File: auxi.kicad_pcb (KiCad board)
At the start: 2 copper layers, 90 x 100 mm, 49 parts

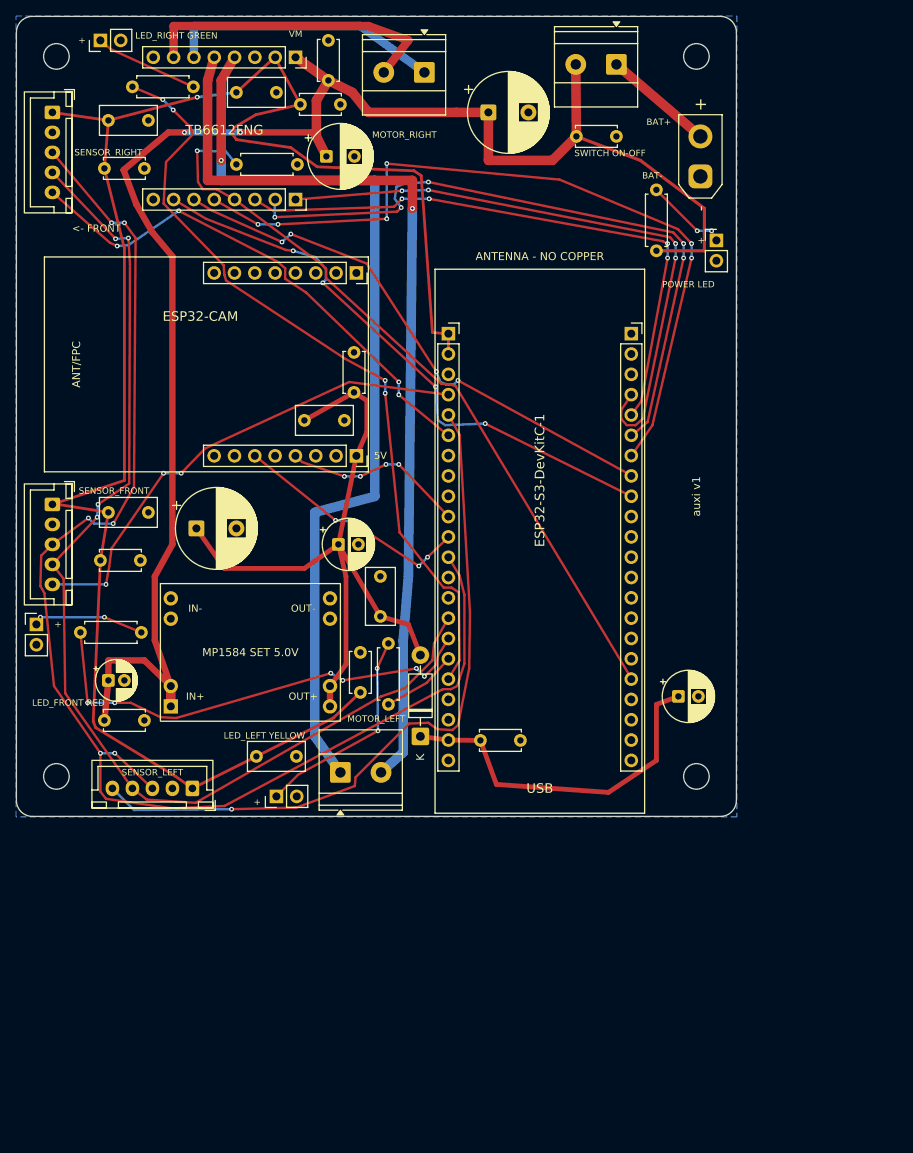
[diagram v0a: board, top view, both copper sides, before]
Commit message: feat(pcb): single-layer 110 x 140 mm board with GND pour, soldered from below
Re-do the PCB as a one-copper-layer board for home etching and hand drilling:

- Copper only on B.Cu with a GND pour; F.Cu has no copper (keepout over the
  whole top face). All parts are THT, mounted on top and soldered from below.
  No vias and no jumper wires: no two tracks cross.
- Board outline 110 x 140 mm (was 90 x 100 mm), M3 holes 5 mm from the corners,
  antenna keepouts for the ESP32-S3 and the ESP32-CAM.
- Track width >= 0.4 mm (0.3 mm only between pads / tight bundles), clearance
  0.2 mm, smallest hole 0.3 mm, default via 1.1 / 0.3 mm. Pad diameter = drill
  + 0.8 mm on every pad hole, enforced by auxi.kicad_dru. Four standard
  footprints copied into auxi.pretty with bigger pads.
- GPIOs reassigned so the signals leave the ESP32 headers in the order of their
  destinations (I2C on GPIO4/5, XSHUT 6/7/15, LEDs 8/9/10, motor signals
  reversed on J3). Schematic updated, ERC clean.
- DRC: 0 violations, 0 unconnected items.
- README.md and CLAUDE.md updated; regenerated schematic PDF, BOM, 1:1 print
  PDF (top, copper, mirrored copper) and renders.

Co-Authored-By: Claude Sonnet 5.5 <noreply@anthropic.com>
Claude-Session: https://claude.ai/code/session_01V1Casvb8MJmuQffuKiRczF
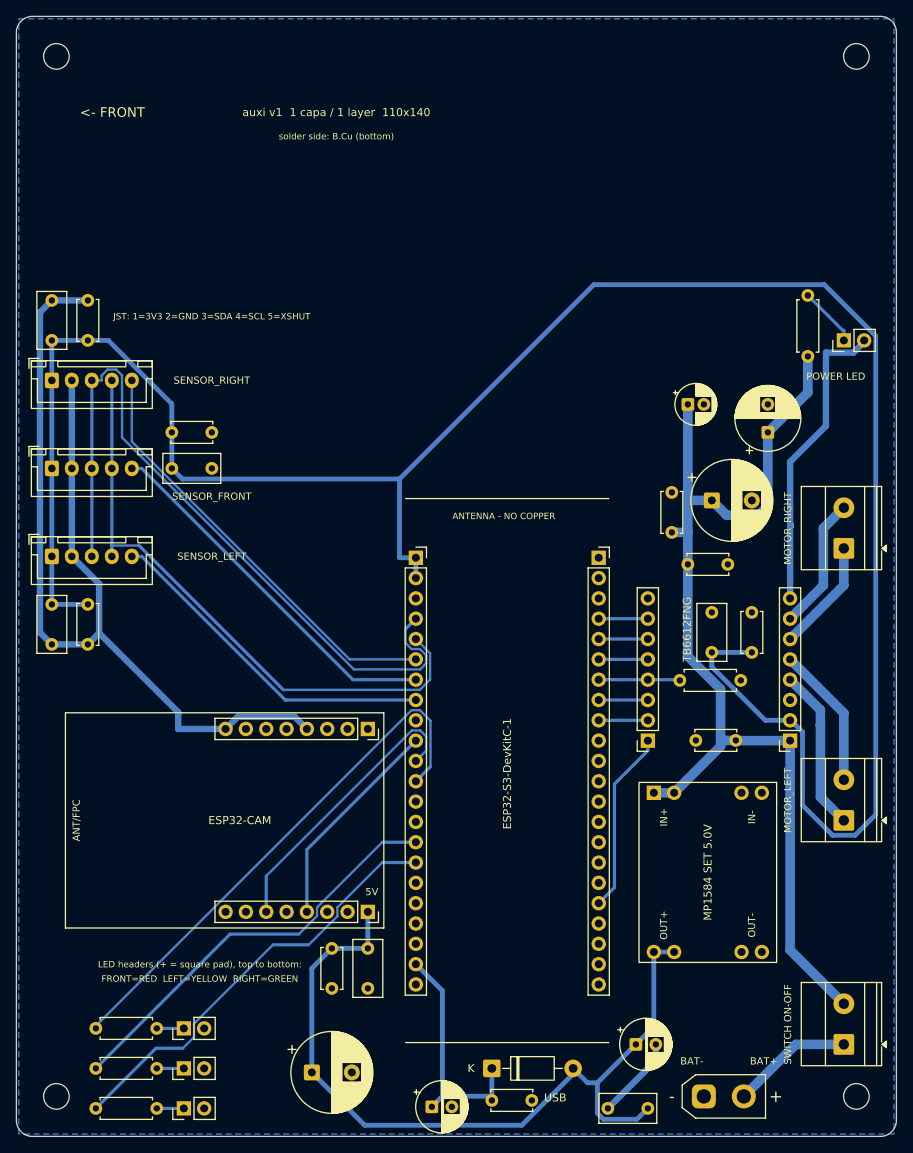
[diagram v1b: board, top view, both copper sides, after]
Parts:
- J_LED_FRONT1, J_LED_LEFT1, J_LED_POWER1, J_LED_RIGHT1: footprint Connector_PinHeader_2.54mm:PinHeader_1x02_P2.54mm_Vertical -> auxi:PinHeader_1x02_P2.54mm_Vertical
- J_SENSOR_FRONT1, J_SENSOR_LEFT1, J_SENSOR_RIGHT1: footprint Connector_JST:JST_XH_B5B-XH-A_1x05_P2.50mm_Vertical -> auxi:JST_XH_B5B-XH-A_1x05_P2.50mm_Vertical
- U_CAM1, U_CAM2, U_TB1, U_TB2: footprint Connector_PinSocket_2.54mm:PinSocket_1x08_P2.54mm_Vertical -> auxi:PinSocket_1x08_P2.54mm_Vertical
- U_ESP_J1, U_ESP_J3: footprint Connector_PinSocket_2.54mm:PinSocket_1x22_P2.54mm_Vertical -> auxi:PinSocket_1x22_P2.54mm_Vertical
- moved J_LED_RIGHT1 133.9 mm to (127.0, 184.0)
- moved R5 127.8 mm to (116.0, 184.0)
- moved J_SWITCH1 125.8 mm to (209.5, 176.0), turned to 90 degrees
- moved J_BAT1 115.0 mm to (192.0, 182.5), turned to 0 degrees
- moved U_TB2 105.4 mm to (202.8, 138.0), turned to 180 degrees
- moved C4 97.0 mm to (196.0, 138.0), turned to 180 degrees
- moved C14 91.8 mm to (193.0, 127.0), turned to 90 degrees
- moved C15 88.8 mm to (198.0, 127.0), turned to 90 degrees
- moved R2 85.0 mm to (189.0, 130.5)
- moved U_TB1 80.7 mm to (185.0, 138.0), turned to 180 degrees
- moved C5 80.2 mm to (190.0, 96.0)
- moved J_MOTOR_RIGHT1 79.3 mm to (209.5, 114.0), turned to 90 degrees
- moved C6 74.7 mm to (188.0, 112.0), turned to 90 degrees
- moved C7 72.7 mm to (183.5, 176.0)
- moved C8 70.0 mm to (185.0, 184.0), turned to 180 degrees
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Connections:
- U_ESP_J1 pad 12: SDA -> LED_FRONT
- U_ESP_J1 pad 15: SCL -> LED_LEFT
- U_ESP_J1 pad 16: LED_FRONT -> LED_RIGHT
- U_ESP_J1 pad 17: LED_LEFT -> (no net)
- U_ESP_J1 pad 18: LED_RIGHT -> (no net)
- U_ESP_J1 pad 4: XSHUT_FRONT -> SDA
- U_ESP_J1 pad 5: XSHUT_LEFT -> SCL
- U_ESP_J1 pad 7: (no net) -> XSHUT_FRONT
- U_ESP_J1 pad 8: (no net) -> XSHUT_LEFT
- U_ESP_J3 pad 18: STBY -> PWMA
- U_ESP_J3 pad 4: PWMA -> PWMB
- U_ESP_J3 pad 5: AIN1 -> BIN2
- U_ESP_J3 pad 6: AIN2 -> BIN1
- U_ESP_J3 pad 7: BIN1 -> STBY
- U_ESP_J3 pad 8: BIN2 -> AIN1
- U_ESP_J3 pad 9: PWMB -> AIN2
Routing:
- net GND: track 0.00 -> 170.2 mm
- net M_L2: track 116.4 -> 17.8 mm, vias 1 -> 0
- net M_L1: track 115.8 -> 20.4 mm, vias 1 -> 0
- net BIN1: track 97.4 -> 6.14 mm, vias 6 -> 0
- net STBY: track 94.5 -> 10.2 mm, vias 1 -> 0
- net AIN2: track 83.7 -> 6.14 mm, vias 5 -> 0
- net +VBAT_SW: track 209.0 -> 133.6 mm, vias 2 -> 0
- net SDA: track 168.1 -> 92.9 mm, vias 6 -> 0
- net AIN1: track 75.0 -> 6.14 mm, vias 4 -> 0
- net PWMB: track 73.0 -> 6.14 mm, vias 4 -> 0
- net SCL: track 138.3 -> 75.6 mm, vias 4 -> 0
- net BIN2: track 68.6 -> 6.14 mm, vias 4 -> 0
- net +3V3: track 222.5 -> 281.8 mm, vias 1 -> 0
- net PWMA: track 77.6 -> 22.9 mm, vias 4 -> 0
- net XSHUT_LEFT: track 88.4 -> 42.9 mm, vias 1 -> 0
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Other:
- board size 90 x 100 mm -> 110 x 140 mm
- board text added: "FRONT=RED LEFT=YELLOW RIGHT=GREEN"
- board text added: "JST: 1=3V3 2=GND 3=SDA 4=SCL 5=XSHUT"
- board text added: "LED headers (+ = square pad), top to bottom:"
- board text added: "auxi v1 1 capa / 1 layer 110x140"
- board text added: "solder side: B.Cu (bottom)"
- board text removed: "+"
- board text removed: "LED_FRONT RED"
- board text removed: "LED_LEFT YELLOW"
- board text removed: "LED_RIGHT GREEN"
- board text removed: "VM"
- board text removed: "auxi v1"

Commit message: feat(pcb): spread the components over the whole board
The first single-layer layout left the top third of the board empty and
crowded the parts toward the bottom edge. The logic block (ESP32-S3, ESP32-CAM,
TB6612FNG, MP1584) moves 26 mm north, the three sensor connectors get a 14 mm
pitch, the power capacitors and the motor/LED connectors use the upper right
corner, and the LED headers, big capacitors, diode, battery and switch are
spaced along the bottom.

- Re-routed on one layer: 224 tracks, 0 vias, no jumper wires.
- DRC: 0 violations, 0 unconnected items. ERC clean. PCB nets match the
  schematic pin by pin. Pin mapping unchanged from the previous commit.
- 55 tracks (377 mm) stay at 0.3 mm where they squeeze between pads.
- README.md, CLAUDE.md and the 1:1 PDF / renders regenerated.

Co-Authored-By: Claude Sonnet 5.5 <noreply@anthropic.com>
Claude-Session: https://claude.ai/code/session_01V1Casvb8MJmuQffuKiRczF
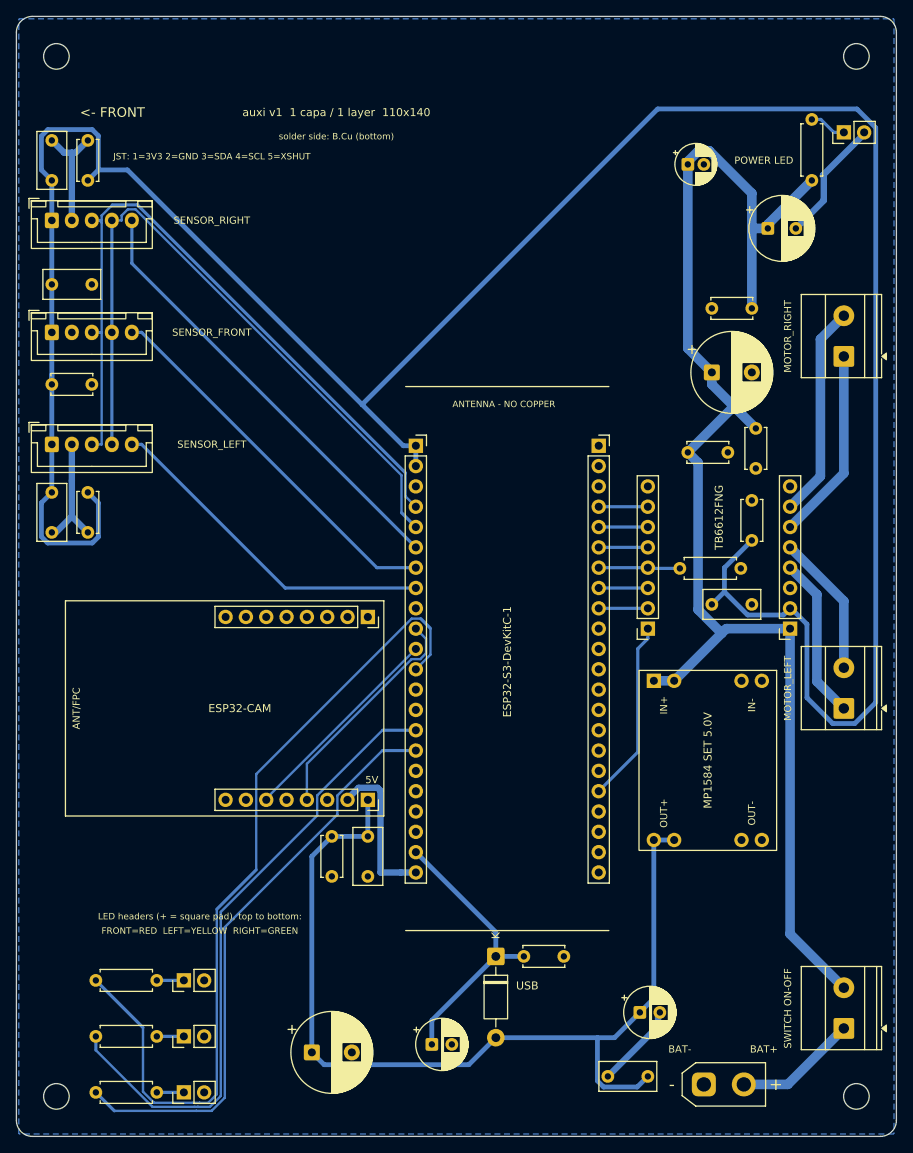
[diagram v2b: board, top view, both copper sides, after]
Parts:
- moved C4 39.1 mm to (198.5, 99.0), turned to -90 degrees
- moved C5 30.0 mm to (190.0, 66.0)
- moved C6 29.7 mm to (198.0, 84.0), turned to 180 degrees
- moved C16 27.5 mm to (110.5, 81.0)
- moved J_LED_POWER1 26.0 mm to (209.5, 62.0)
- moved C3 25.5 mm to (200.0, 74.0), turned to 0 degrees
- moved J_MOTOR_RIGHT1 24.0 mm to (209.5, 90.0)
- moved R1 22.0 mm to (205.5, 68.0)
- moved C20 20.0 mm to (110.5, 68.0)
- moved C21 20.0 mm to (115.0, 68.0)
- moved J_SENSOR_RIGHT1 20.0 mm to (110.5, 73.0)
- moved C10 18.4 mm to (169.5, 165.0)
- moved J_SENSOR_FRONT1 17.0 mm to (110.5, 87.0)
- moved C17 16.2 mm to (110.5, 93.5)
- moved C1 16.0 mm to (193.0, 92.0)
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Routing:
- net GND: track 170.2 -> 75.4 mm
- net +3V3: track 281.8 -> 331.9 mm
- net +VBAT_SW: track 133.6 -> 172.2 mm
- net LED_FRONT: track 67.4 -> 104.9 mm
- net LED_LEFT: track 52.3 -> 79.1 mm
- net LED_RIGHT: track 54.4 -> 73.5 mm
- net +5V: track 100.9 -> 118.8 mm
- net SCL: track 75.6 -> 86.1 mm
- net M_R1: track 16.7 -> 26.7 mm
- net M_R2: track 14.1 -> 24.1 mm
- net UART_CAM_TO_ESP: track 35.9 -> 26.6 mm
- net +5V_ESP: track 29.9 -> 35.0 mm
- net LED_POWER_A: track 7.56 -> 4.67 mm
- net SDA: track 92.9 -> 90.8 mm
- net UART_ESP_TO_CAM: track 27.0 -> 28.7 mm
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
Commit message: Move ESP32-S3 so its USB end sits ~5 mm from the board edge and re-route
The USB port is now reachable from the side. The board was re-placed
and re-routed on a single layer (199 tracks, DRC 0 violations, 0
unconnected). J_LED_POWER moved off the corner so the +3V3 track can
reach the TB6612 VCC pin. Docs, PDFs and renders regenerated.

Co-Authored-By: Claude Sonnet 5.5 <noreply@anthropic.com>
Claude-Session: https://claude.ai/code/session_01V1Casvb8MJmuQffuKiRczF
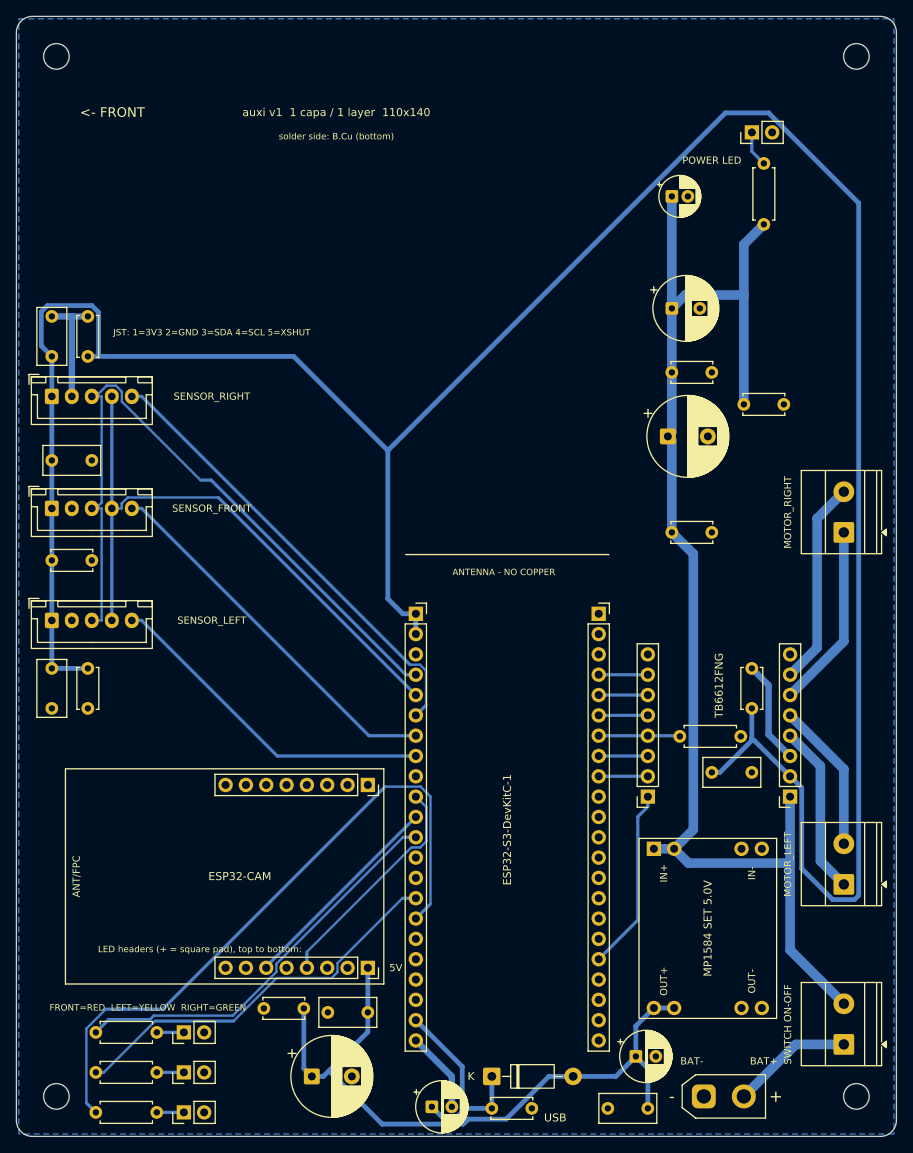
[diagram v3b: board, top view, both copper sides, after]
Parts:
- moved C12 22.0 mm to (150.0, 172.0), turned to 180 degrees
- moved C16 22.0 mm to (110.5, 103.0)
- moved C17 22.0 mm to (110.5, 115.5)
- moved C18 22.0 mm to (110.5, 129.0)
- moved C19 22.0 mm to (115.0, 129.0)
- moved C20 22.0 mm to (110.5, 90.0)
- moved C21 22.0 mm to (115.0, 90.0)
- moved J_MOTOR_LEFT1 22.0 mm to (209.5, 156.0)
- moved J_MOTOR_RIGHT1 22.0 mm to (209.5, 112.0)
- moved J_SENSOR_FRONT1 22.0 mm to (110.5, 109.0)
- moved J_SENSOR_LEFT1 22.0 mm to (110.5, 123.0)
- moved J_SENSOR_RIGHT1 22.0 mm to (110.5, 95.0)
- moved C13 21.8 mm to (142.0, 171.5), turned to 180 degrees
- moved C14 21.0 mm to (193.0, 142.0)
- moved C15 21.0 mm to (198.0, 134.0)
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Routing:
- net LED_FRONT: track 104.9 -> 51.0 mm
- net GND: track 75.4 -> 37.6 mm
- net +5V: track 118.8 -> 88.0 mm
- net LED_LEFT: track 79.1 -> 49.7 mm
- net LED_RIGHT: track 73.5 -> 83.0 mm
- net SCL: track 86.1 -> 77.2 mm
- net +5V_ESP: track 35.0 -> 26.2 mm
- net +VBAT_SW: track 172.2 -> 163.7 mm
- net +3V3: track 331.9 -> 336.6 mm
- net SDA: track 90.8 -> 88.2 mm
- net XSHUT_RIGHT: track 55.6 -> 57.1 mm
- net M_R1: track 26.7 -> 25.7 mm
- net M_L2: track 17.8 -> 18.8 mm
- net M_L1: track 20.4 -> 21.4 mm
- net M_R2: track 24.1 -> 23.1 mm

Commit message: Re-layout for the real orientation: 110 mm side is the front, ESP32-S3 USB at the rear edge
- ESP32-CAM at the front-left corner (camera looking forward), sensors
  along the front edge, ESP32-S3 at the rear with the USB end 1 mm from
  the edge, TB6612 and motor terminals on the east side, MP1584 on the
  west side.
- GPIO mapping changed again: XSHUT 4/5/6, SCL 7, SDA 15, UART RX 17 and
  TX 18 (schematic labels updated, ERC clean, PCB nets match the schematic).
- Board re-routed on one layer: 197 tracks, DRC 0 errors, 0 unconnected.
- README, CLAUDE.md, PDFs, renders and DRC report regenerated.

Co-Authored-By: Claude Sonnet 5.5 <noreply@anthropic.com>
Claude-Session: https://claude.ai/code/session_01V1Casvb8MJmuQffuKiRczF
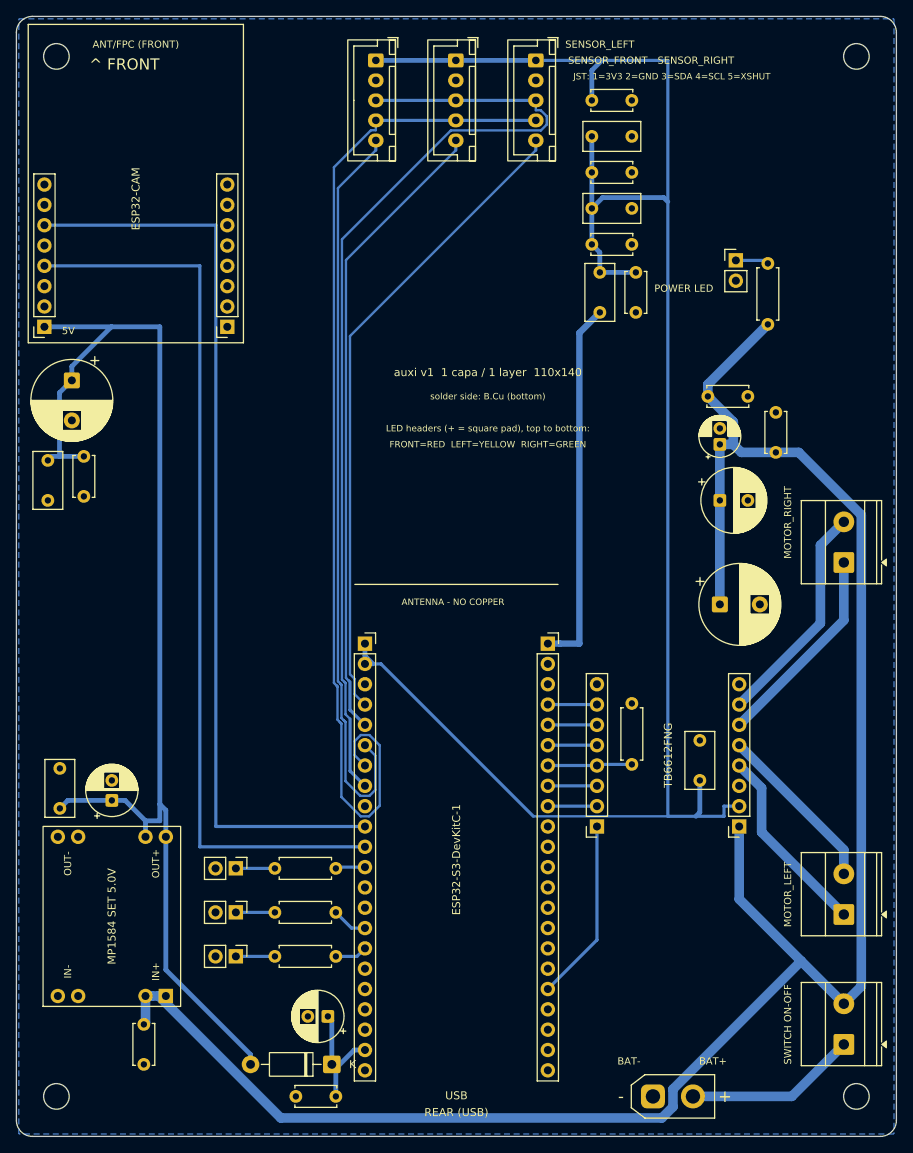
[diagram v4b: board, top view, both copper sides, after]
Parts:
- moved C4 107.8 mm to (122.0, 173.5), turned to -90 degrees
- moved C11 92.0 mm to (113.0, 93.0), turned to -90 degrees
- moved U_CAM1 89.8 mm to (109.6, 86.3), turned to 180 degrees
- moved C18 88.7 mm to (178.0, 71.5), turned to 0 degrees
- moved C17 83.1 mm to (178.0, 67.0)
- moved C8 82.5 mm to (111.5, 146.5), turned to 90 degrees
- moved C19 82.3 mm to (178.0, 76.0), turned to 0 degrees
- moved J_SENSOR_LEFT1 80.9 mm to (151.0, 53.0), turned to -90 degrees
- moved C12 79.8 mm to (110.0, 103.0), turned to -90 degrees
- moved C16 78.7 mm to (178.0, 62.5)
- moved C15 78.6 mm to (178.0, 58.0), turned to 0 degrees
- moved J_SENSOR_FRONT1 75.4 mm to (161.0, 53.0), turned to -90 degrees
- moved U_MP1584 74.5 mm to (118.0, 160.0), turned to 90 degrees
- moved C13 74.3 mm to (114.5, 102.5), turned to -90 degrees
- moved J_SENSOR_RIGHT1 73.6 mm to (171.0, 53.0), turned to -90 degrees
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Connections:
- U_ESP_J1 pad 10: UART_ESP_TO_CAM -> UART_CAM_TO_ESP
- U_ESP_J1 pad 11: UART_CAM_TO_ESP -> UART_ESP_TO_CAM
- U_ESP_J1 pad 4: SDA -> XSHUT_RIGHT
- U_ESP_J1 pad 5: SCL -> XSHUT_FRONT
- U_ESP_J1 pad 6: XSHUT_RIGHT -> XSHUT_LEFT
- U_ESP_J1 pad 7: XSHUT_FRONT -> SCL
- U_ESP_J1 pad 8: XSHUT_LEFT -> SDA
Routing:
- net +3V3: track 336.6 -> 232.3 mm
- net +VBAT_SW: track 163.7 -> 252.5 mm
- net UART_CAM_TO_ESP: track 26.6 -> 115.2 mm
- net UART_ESP_TO_CAM: track 28.8 -> 112.7 mm
- net LED_RIGHT: track 83.0 -> 4.05 mm
- net +5V: track 88.0 -> 153.0 mm
- net SCL: track 77.2 -> 129.4 mm
- net XSHUT_LEFT: track 42.5 -> 93.9 mm
- net LED_FRONT: track 51.0 -> 3.71 mm
- net LED_LEFT: track 49.7 -> 4.45 mm
- net SDA: track 88.2 -> 125.2 mm
- net XSHUT_FRONT: track 47.3 -> 80.0 mm
- net XSHUT_RIGHT: track 57.1 -> 80.9 mm
- net +5V_ESP: track 26.2 -> 15.0 mm
- net GND: track 37.6 -> 46.4 mm
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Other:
- board text added: "ANT/FPC (FRONT)"
- board text added: "REAR (USB)"
- board text added: "^ FRONT"
- board text removed: "<- FRONT"
- board text removed: "ANT/FPC"
